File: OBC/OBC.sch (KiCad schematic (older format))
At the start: 9 parts, among them J0 Raspberry_Pi_2_3, J1 Power, J2 Terminal_5V0, J3 PB_5V0, J4 I2C, J5 PB_3V3, J6 I2C, J7 CSP_I2C, U0 Payload

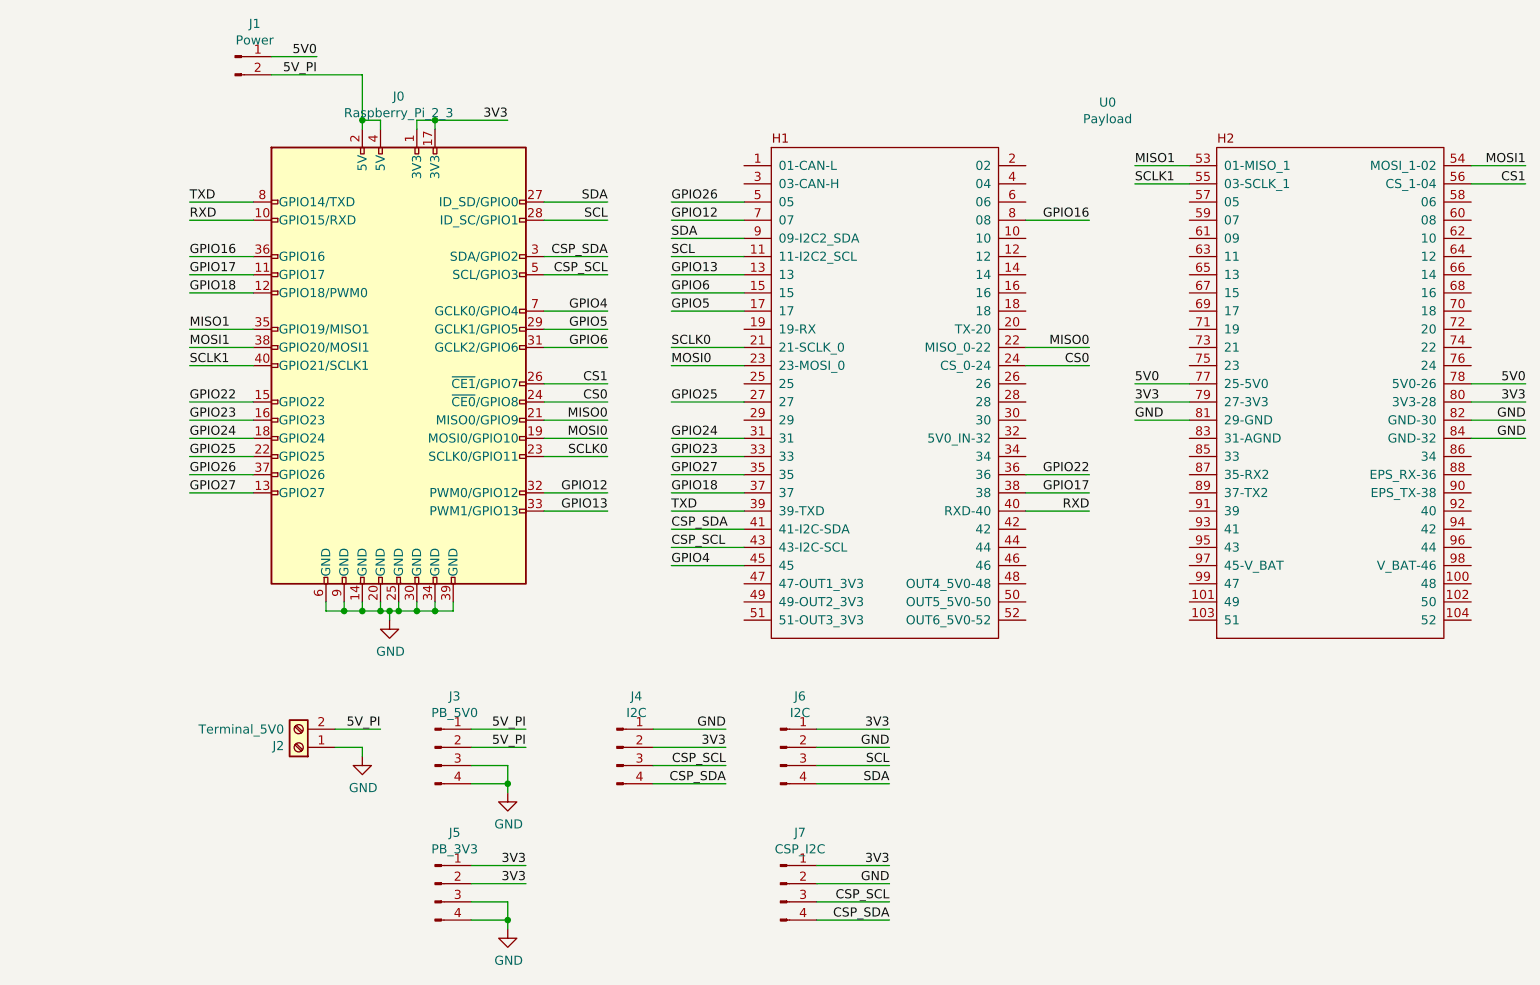
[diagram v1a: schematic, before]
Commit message: Added sensors to the OBC. Replaced the four-pin-picoblade connectors with six-pin-picoblade connectors. Added some vias to cut through them a hole for the camera connector.
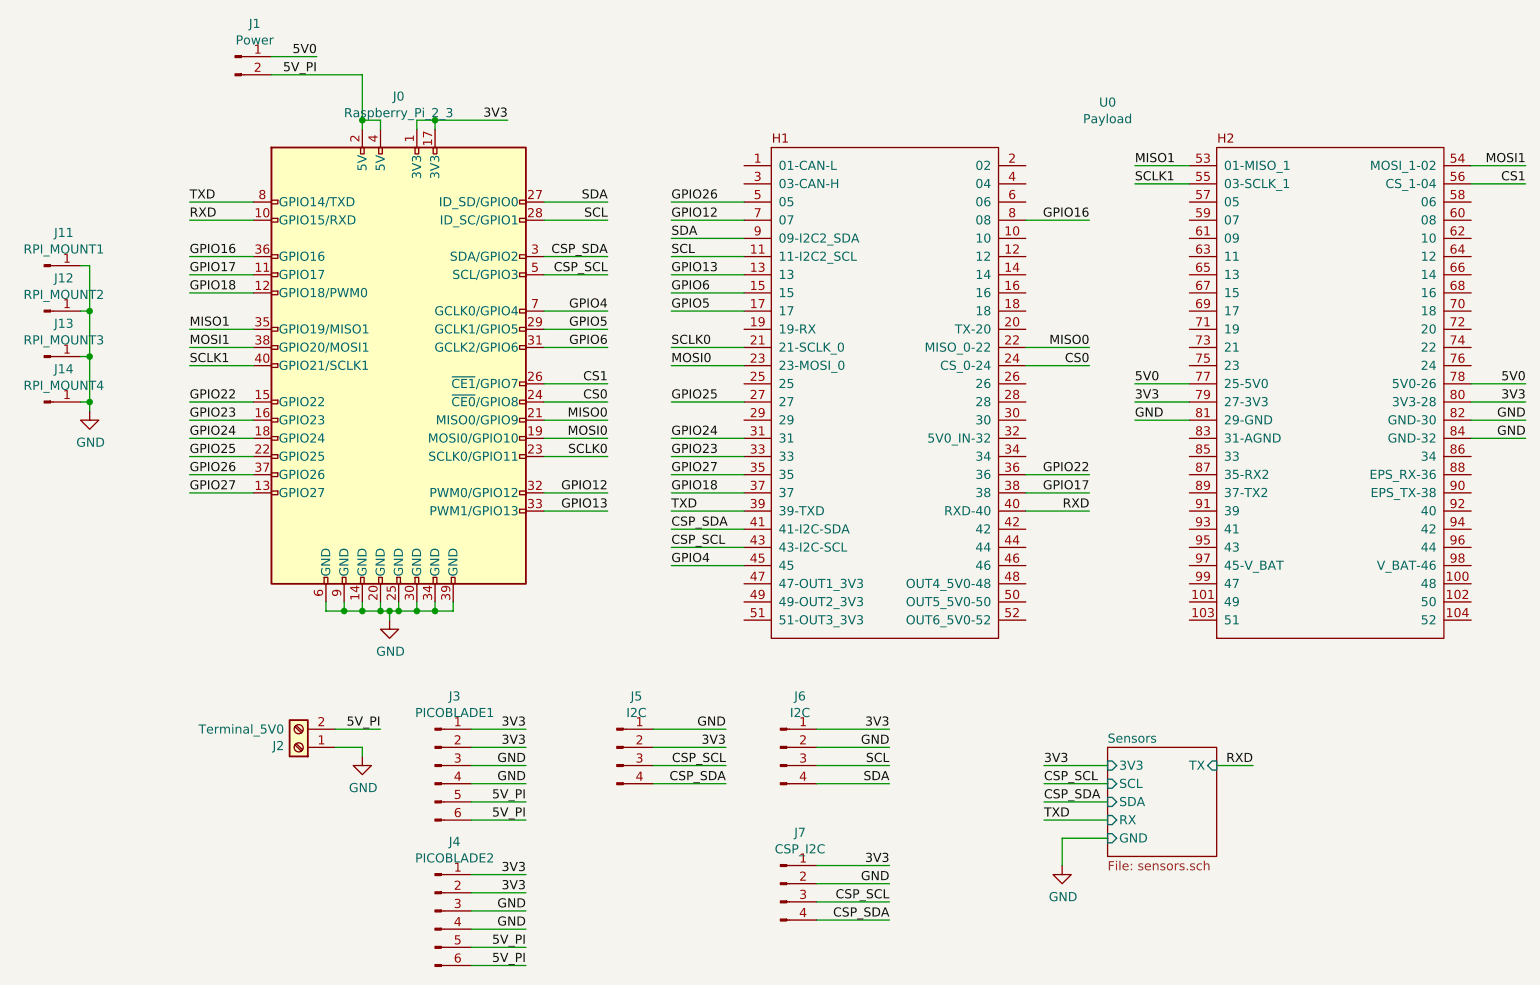
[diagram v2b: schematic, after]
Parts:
- removed J3: PB_5V0, Connector_Molex:Molex_PicoBlade_53048-0410_1x04_P1.25mm_Horizontal, symbol Connector:Conn_01x04_Male
- removed J5: PB_3V3, Connector_Molex:Molex_PicoBlade_53048-0410_1x04_P1.25mm_Horizontal, symbol Connector:Conn_01x04_Male
- added J11: RPI_MOUNT1, Connector_PinHeader_2.54mm:PinHeader_1x01_P2.54mm_Vertical, symbol Connector:Conn_01x01_Male
- added J12: RPI_MOUNT2, Connector_PinHeader_2.54mm:PinHeader_1x01_P2.54mm_Vertical, symbol Connector:Conn_01x01_Male
- added J13: RPI_MOUNT3, Connector_PinHeader_2.54mm:PinHeader_1x01_P2.54mm_Vertical, symbol Connector:Conn_01x01_Male
- added J14: RPI_MOUNT4, Connector_PinHeader_2.54mm:PinHeader_1x01_P2.54mm_Vertical, symbol Connector:Conn_01x01_Male
- added J3: PICOBLADE1, Connector_Molex:Molex_PicoBlade_53048-0610_1x06_P1.25mm_Horizontal, symbol Connector:Conn_01x06_Male
- added J4: PICOBLADE2, Connector_Molex:Molex_PicoBlade_53048-0610_1x06_P1.25mm_Horizontal, symbol Connector:Conn_01x06_Male
- renumbered J4 to J5
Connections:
- net 3V3: now also J3.1 (Pin_1), J3.2 (Pin_2), J4.1 (Pin_1), J4.2 (Pin_2)
- net 5V_PI: now also J3.5 (Pin_5), J3.6 (Pin_6), J4.5 (Pin_5), J4.6 (Pin_6)
- net GND: now also J11.1 (Pin_1), J12.1 (Pin_1), J13.1 (Pin_1), J14.1 (Pin_1), J3.3 (Pin_3), J3.4 (Pin_4), J4.3 (Pin_3), J4.4 (Pin_4)
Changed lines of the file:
@@
 $Descr A4 11693 8268
 encoding utf-8
-Sheet 1 1
+Sheet 1 2
 Title ""
 Date ""
@@
 $EndComp
 $Comp
-L Connector:Conn_01x04_Male J3
-U 1 1 5D262D74
-P 4350 5100
-F 0 "J3" H 4458 5381 50  0000 C CNN
-F 1 "PB_5V0" H 4458 5290 50  0000 C CNN
-F 2 "Connector_Molex:Molex_PicoBlade_53048-0410_1x04_P1.25mm_Horizontal" H 4350 5100 50  0001 C CNN
-F 3 "~" H 4350 5100 50  0001 C CNN
-	1    4350 5100
-	1    0    0    -1
-$EndComp
-$Comp
 L Connector:Conn_01x04_Male J6
 U 1 1 5D2667C7
@@
 Text Label 4050 5000 2    50   ~ 0
 5V_PI
-Text Label 4850 5000 2    50   ~ 0
+Text Label 4850 5400 2    50   ~ 0
 5V_PI
-Text Label 4850 5100 2    50   ~ 0
+Text Label 4850 5500 2    50   ~ 0
 5V_PI
-Text Label 4850 5750 2    50   ~ 0
-3V3
-Text Label 4850 5850 2    50   ~ 0
+Text Label 4850 5800 2    50   ~ 0
+3V3
+Text Label 4850 5900 2    50   ~ 0
 3V3
 Wire Wire Line
@@
 	4550 5100 4850 5100
 Wire Wire Line
-	4850 5750 4550 5750
-Wire Wire Line
-	4550 5850 4850 5850
-Wire Wire Line
-	4550 5300 4750 5300
-Wire Wire Line
-	4750 5300 4750 5350
-Wire Wire Line
-	4550 5200 4750 5200
-Wire Wire Line
-	4750 5200 4750 5300
-Connection ~ 4750 5300
-Wire Wire Line
-	4550 5950 4750 5950
-Wire Wire Line
-	4750 5950 4750 6050
-Wire Wire Line
-	4550 6050 4750 6050
-Connection ~ 4750 6050
-Wire Wire Line
-	4750 6050 4750 6100
-$Comp
-L power:GND #PWR0104
-U 1 1 5D26A2CE
-P 4750 5350
-F 0 "#PWR0104" H 4750 5100 50  0001 C CNN
-F 1 "GND" H 4755 5177 50  0000 C CNN
-F 2 "" H 4750 5350 50  0001 C CNN
-F 3 "" H 4750 5350 50  0001 C CNN
-	1    4750 5350
-	1    0    0    -1
-$EndComp
-$Comp
-L power:GND #PWR0105
-U 1 1 5D26A590
-P 4750 6100
-F 0 "#PWR0105" H 4750 5850 50  0001 C CNN
-F 1 "GND" H 4755 5927 50  0000 C CNN
-F 2 "" H 4750 6100 50  0001 C CNN
-F 3 "" H 4750 6100 50  0001 C CNN
-	1    4750 6100
-	1    0    0    -1
-$EndComp
+	4850 5800 4550 5800
+Wire Wire Line
+	4550 5900 4850 5900
 Text Label 6850 6050 2    50   ~ 0
 CSP_SDA
@@
 Wire Wire Line
 	6850 5950 6450 5950
-$Comp
-L Connector:Conn_01x04_Male J5
-U 1 1 5D266258
-P 4350 5850
-F 0 "J5" H 4458 6131 50  0000 C CNN
-F 1 "PB_3V3" H 4458 6040 50  0000 C CNN
-F 2 "Connector_Molex:Molex_PicoBlade_53048-0410_1x04_P1.25mm_Horizontal" H 4350 5850 50  0001 C CNN
-F 3 "~" H 4350 5850 50  0001 C CNN
-	1    4350 5850
-	1    0    0    -1
-$EndComp
 Wire Wire Line
 	6450 6050 6850 6050
@@
 3V3
 $Comp
-L Connector:Conn_01x04_Male J4
+L Connector:Conn_01x04_Male J5
 U 1 1 5D2773BC
 P 5350 5100
-F 0 "J4" H 5458 5381 50  0000 C CNN
+F 0 "J5" H 5458 5381 50  0000 C CNN
 F 1 "I2C" H 5458 5290 50  0000 C CNN
 F 2 "Connector_PinHeader_2.54mm:PinHeader_1x04_P2.54mm_Vertical" H 5350 5100 50  0001 C CNN
@@
 Wire Wire Line
 	5950 5000 5550 5000
+$Sheet
+S 8050 5100 600  600
+U 5D2760D4
+F0 "Sensors" 50
+F1 "sensors.sch" 50
+F2 "3V3" I L 8050 5200 50
+F3 "GND" I L 8050 5600 50
+F4 "SCL" I L 8050 5300 50
+F5 "SDA" I L 8050 5400 50
+F6 "RX" I L 8050 5500 50
+F7 "TX" I R 8650 5200 50
+$EndSheet
+Text Label 7700 5200 0    50   ~ 0
+3V3
+Text Label 7700 5300 0    50   ~ 0
+CSP_SCL
+Text Label 7700 5400 0    50   ~ 0
+CSP_SDA
+Text Label 7700 5500 0    50   ~ 0
+TXD
+Text Label 8850 5200 2    50   ~ 0
+RXD
+Wire Wire Line
+	8850 5200 8650 5200
+Wire Wire Line
+	7800 5600 7800 5750
+$Comp
+L power:GND #PWR0103
+U 1 1 5D278E16
+P 7800 5750
+F 0 "#PWR0103" H 7800 5500 50  0001 C CNN
+F 1 "GND" H 7805 5577 50  0000 C CNN
+F 2 "" H 7800 5750 50  0001 C CNN
+F 3 "" H 7800 5750 50  0001 C CNN
+	1    7800 5750
+	1    0    0    -1
+$EndComp
+Wire Wire Line
+	7700 5200 8050 5200
+Wire Wire Line
+	7700 5300 8050 5300
+Wire Wire Line
+	7700 5500 8050 5500
+Wire Wire Line
+	7700 5400 8050 5400
+Wire Wire Line
+	7800 5600 8050 5600
+$Comp
+L Connector:Conn_01x06_Male J3
+U 1 1 5D27C9CC
+P 4350 5200
+F 0 "J3" H 4458 5581 50  0000 C CNN
+F 1 "PICOBLADE1" H 4458 5490 50  0000 C CNN
+F 2 "Connector_Molex:Molex_PicoBlade_53048-0610_1x06_P1.25mm_Horizontal" H 4350 5200 50  0001 C CNN
+F 3 "~" H 4350 5200 50  0001 C CNN
+	1    4350 5200
+	1    0    0    -1
+$EndComp
+$Comp
+L Connector:Conn_01x06_Male J4
+U 1 1 5D27D485
+P 4350 6000
+F 0 "J4" H 4458 6381 50  0000 C CNN
+F 1 "PICOBLADE2" H 4458 6290 50  0000 C CNN
+F 2 "Connector_Molex:Molex_PicoBlade_53048-0610_1x06_P1.25mm_Horizontal" H 4350 6000 50  0001 C CNN
+F 3 "~" H 4350 6000 50  0001 C CNN
+	1    4350 6000
+	1    0    0    -1
+$EndComp
+Wire Wire Line
+	4550 5200 4850 5200
+Wire Wire Line
+	4550 5300 4850 5300
+Wire Wire Line
+	4850 5500 4550 5500
+Wire Wire Line
+	4550 5400 4850 5400
+Text Label 4850 5200 2    50   ~ 0
+GND
+Text Label 4850 5300 2    50   ~ 0
+GND
+Text Label 4850 5000 2    50   ~ 0
+3V3
+Text Label 4850 5100 2    50   ~ 0
+3V3
+Wire Wire Line
+	4550 6200 4850 6200
+Wire Wire Line
+	4850 6300 4550 6300
+Wire Wire Line
+	4550 6100 4850 6100
+Wire Wire Line
+	4550 6000 4850 6000
+Text Label 4850 6300 2    50   ~ 0
+5V_PI
+Text Label 4850 6200 2    50   ~ 0
+5V_PI
+Text Label 4850 6000 2    50   ~ 0
+GND
+Text Label 4850 6100 2    50   ~ 0
+GND
+$Comp
+L Connector:Conn_01x01_Male J11
+U 1 1 5D290C4C
+P 2200 2450
+F 0 "J11" H 2308 2631 50  0000 C CNN
+F 1 "RPI_MOUNT1" H 2308 2540 50  0000 C CNN
+F 2 "Connector_PinHeader_2.54mm:PinHeader_1x01_P2.54mm_Vertical" H 2200 2450 50  0001 C CNN
+F 3 "~" H 2200 2450 50  0001 C CNN
+	1    2200 2450
+	1    0    0    -1
+$EndComp
+$Comp
+L Connector:Conn_01x01_Male J12
+U 1 1 5D291331
+P 2200 2700
+F 0 "J12" H 2308 2881 50  0000 C CNN
+F 1 "RPI_MOUNT2" H 2308 2790 50  0000 C CNN
+F 2 "Connector_PinHeader_2.54mm:PinHeader_1x01_P2.54mm_Vertical" H 2200 2700 50  0001 C CNN
+F 3 "~" H 2200 2700 50  0001 C CNN
+	1    2200 2700
+	1    0    0    -1
+$EndComp
+$Comp
+L Connector:Conn_01x01_Male J13
+U 1 1 5D29151A
+P 2200 2950
+F 0 "J13" H 2308 3131 50  0000 C CNN
+F 1 "RPI_MOUNT3" H 2308 3040 50  0000 C CNN
+F 2 "Connector_PinHeader_2.54mm:PinHeader_1x01_P2.54mm_Vertical" H 2200 2950 50  0001 C CNN
+F 3 "~" H 2200 2950 50  0001 C CNN
+	1    2200 2950
+	1    0    0    -1
+$EndComp
+$Comp
+L Connector:Conn_01x01_Male J14
+U 1 1 5D29180F
+P 2200 3200
+F 0 "J14" H 2308 3381 50  0000 C CNN
+F 1 "RPI_MOUNT4" H 2308 3290 50  0000 C CNN
+F 2 "Connector_PinHeader_2.54mm:PinHeader_1x01_P2.54mm_Vertical" H 2200 3200 50  0001 C CNN
+F 3 "~" H 2200 3200 50  0001 C CNN
+	1    2200 3200
+	1    0    0    -1
+$EndComp
+Wire Wire Line
+	2450 3200 2400 3200
+Wire Wire Line
+	2400 2450 2450 2450
+Wire Wire Line
+	2450 2450 2450 2700
+Wire Wire Line
+	2400 2700 2450 2700
+Connection ~ 2450 2700
+Wire Wire Line
+	2450 2700 2450 2950
+Wire Wire Line
+	2400 2950 2450 2950
+Connection ~ 2450 2950
+Wire Wire Line
+	2450 2950 2450 3200
+Wire Wire Line
+	2450 3200 2450 3250
+Connection ~ 2450 3200
+$Comp
+L power:GND #PWR0104
+U 1 1 5D29519F
+P 2450 3250
+F 0 "#PWR0104" H 2450 3000 50  0001 C CNN
+F 1 "GND" H 2455 3077 50  0000 C CNN
+F 2 "" H 2450 3250 50  0001 C CNN
+F 3 "" H 2450 3250 50  0001 C CNN
+	1    2450 3250
+	1    0    0    -1
+$EndComp
 $EndSCHEMATC
